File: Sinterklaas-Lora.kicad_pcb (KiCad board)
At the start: 2 copper layers, 80 x 100 mm, 1 part, among them U1 Pico

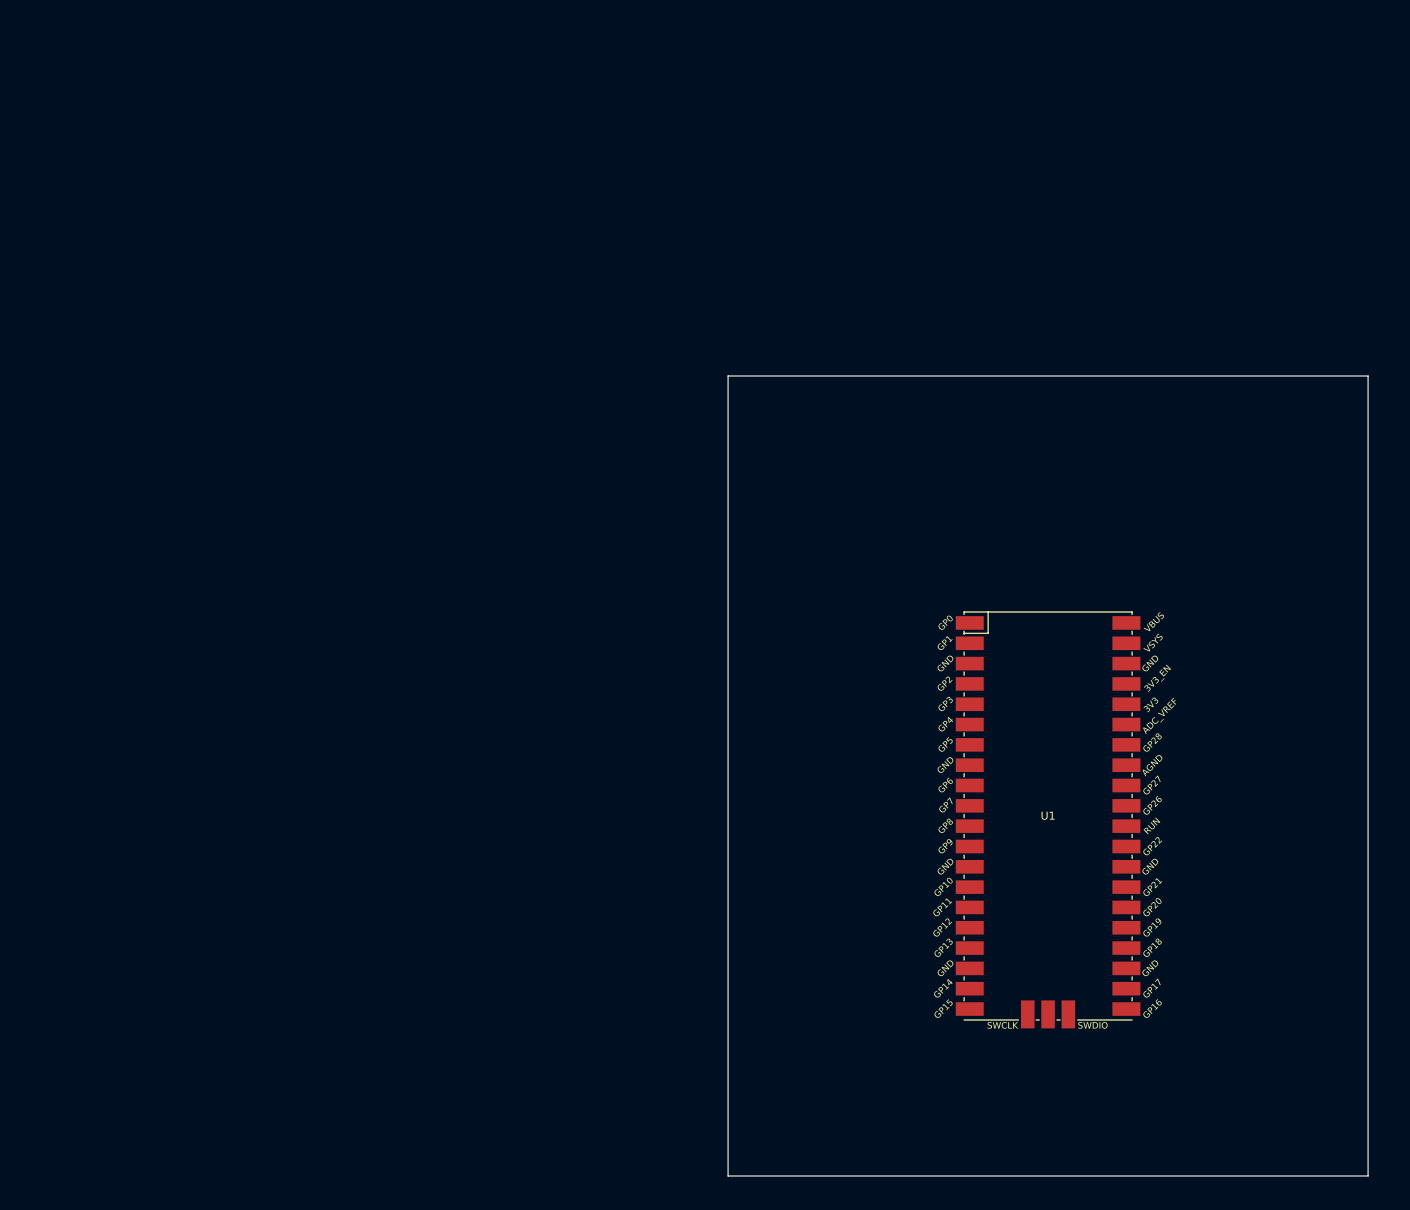
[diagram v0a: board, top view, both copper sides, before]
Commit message: Added battery holder
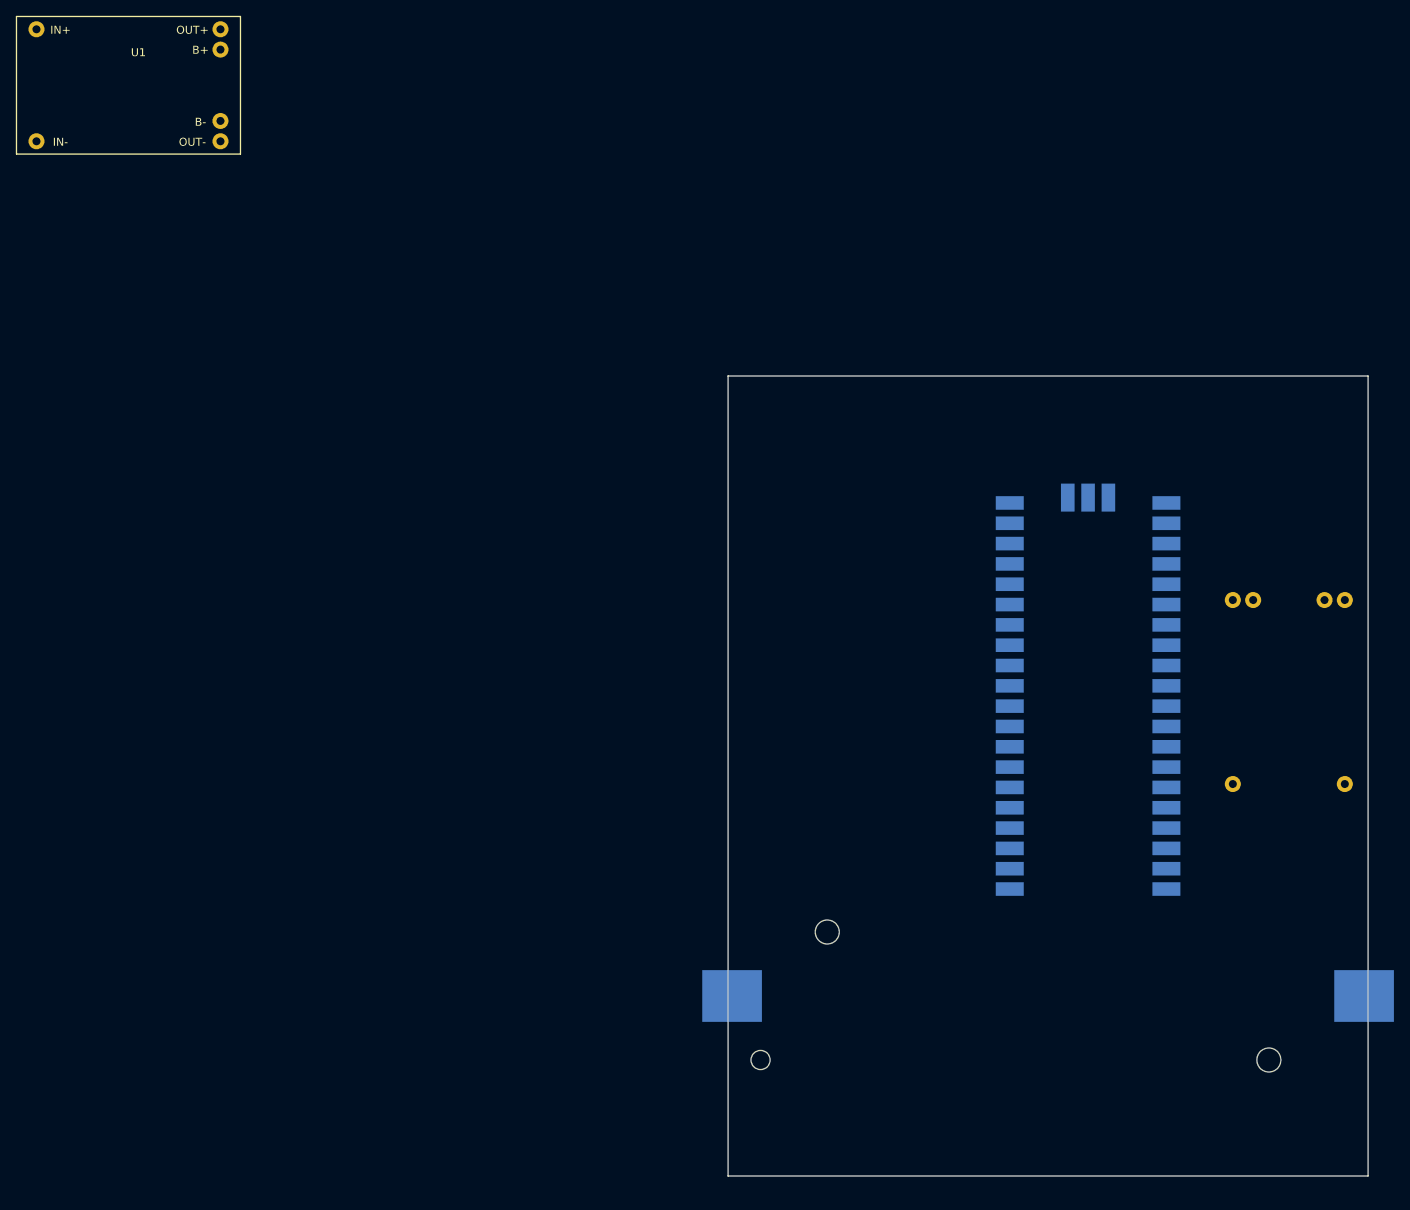
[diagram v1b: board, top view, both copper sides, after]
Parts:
- added BT1: Battery_Cell, Pi_pico:1042P, B.Cu at (172.5, 132.5)
- added U1: TP4056, Pi_pico:TP4056-Module, F.Cu at (1.05, 17.3)
- added U1: TP4056, Pi_pico:TP4056-Module, B.Cu at (151.5, 98.5)
- U2: renamed from U1; moved to B.Cu
- moved U2 15.8 mm to (135.0, 85.0)

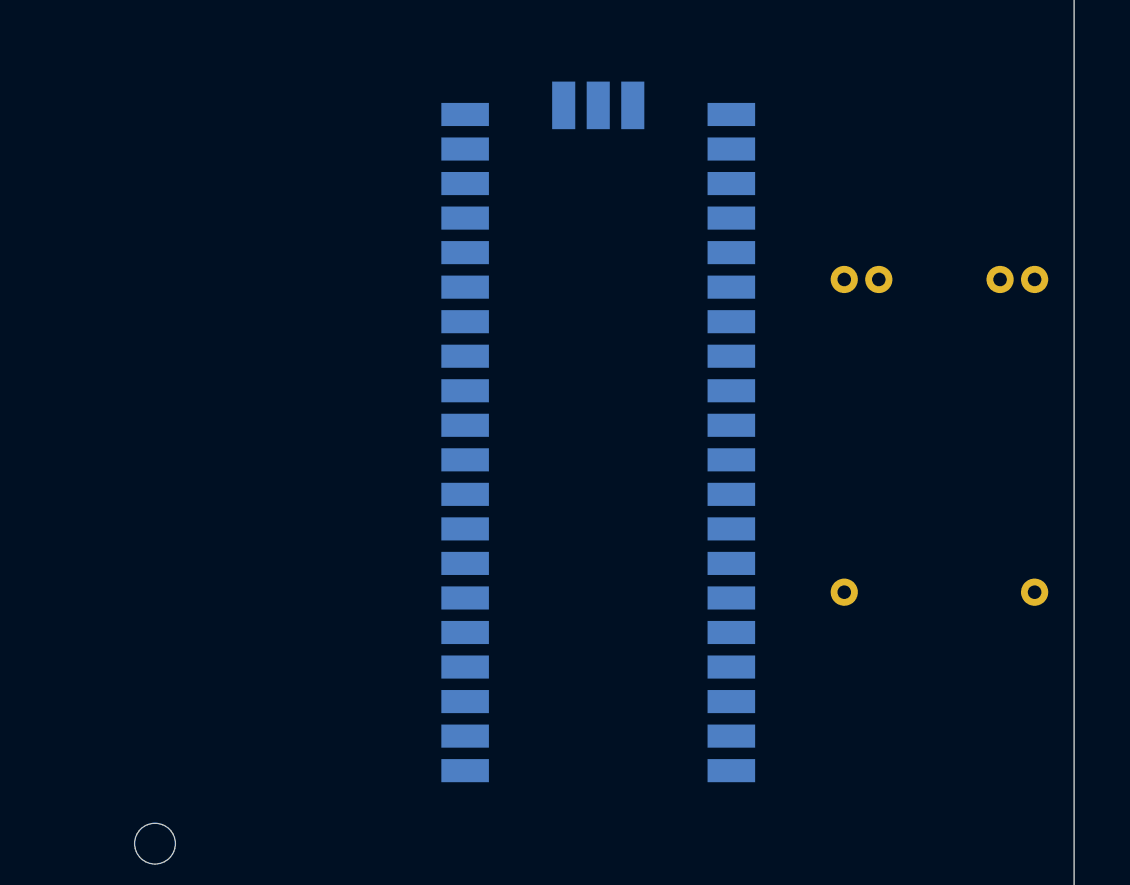
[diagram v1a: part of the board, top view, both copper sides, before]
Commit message: Added eByte E22-900M22S module to schematic
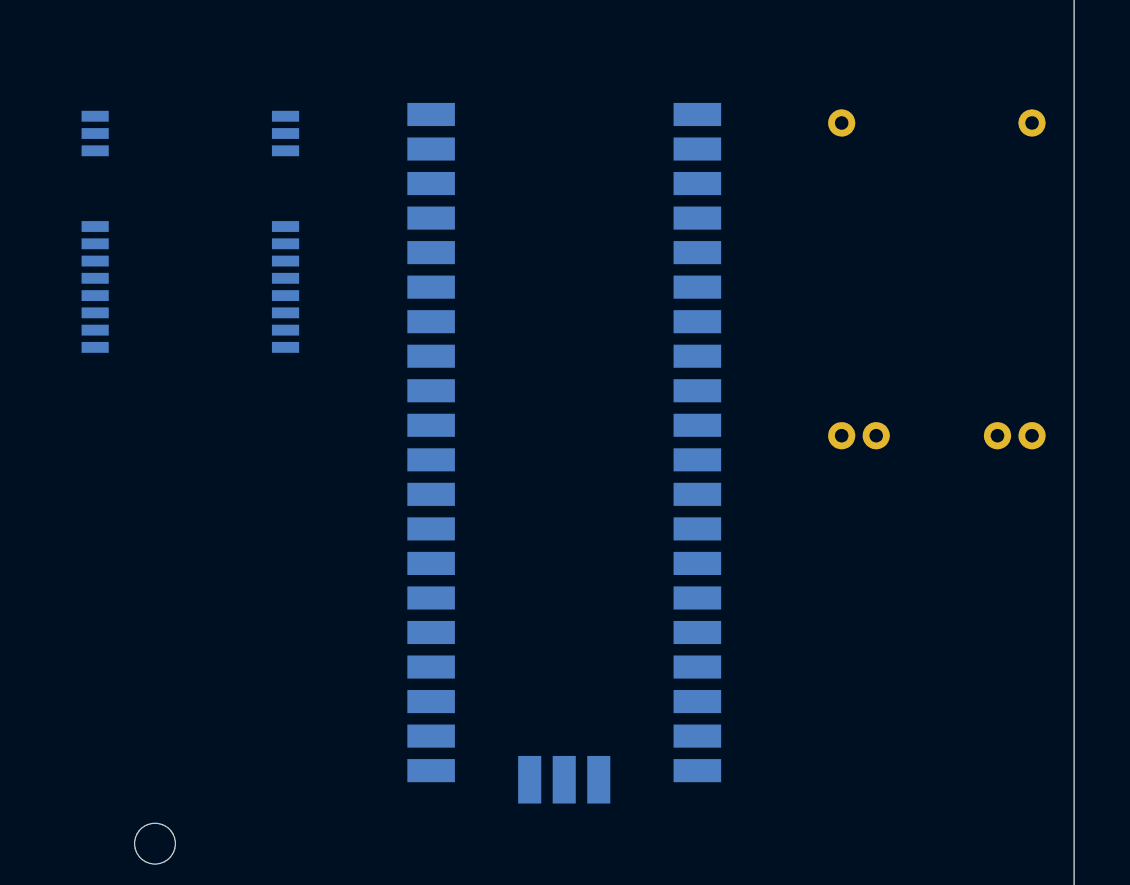
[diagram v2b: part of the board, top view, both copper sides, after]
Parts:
- added IC1: E22-900M22S, Pi_pico:E22-900M22S, B.Cu at (105.0, 70.0)
- moved U1 43.0 mm to (168.5, 59.0), turned to -90 degrees
- moved U2 2.50 mm to (132.5, 85.0), turned to 180 degrees
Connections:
- net Net-(BT1-Pad1) renamed VCC

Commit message: Added text
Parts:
- removed the U1 at (1.05, 17.3)
- added Q1: DMG2302U, Package_TO_SOT_SMD:SOT-23, B.Cu at (117.5, 62.5)
- moved U1 2.61 mm to (166.0, 59.7)
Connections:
- net VCC renamed Net-(BT1-Pad1)
- IC1 pad 1: Net-(IC1-Pad1) -> GND
- IC1 pad 10: Net-(IC1-Pad1) -> GND
- IC1 pad 11: Net-(IC1-Pad1) -> GND
- IC1 pad 12: Net-(IC1-Pad1) -> GND
- IC1 pad 13: unconnected-(IC1-Pad13) -> Net-(IC1-Pad13)
- IC1 pad 14: unconnected-(IC1-Pad14) -> Net-(IC1-Pad14)
- IC1 pad 16: unconnected-(IC1-Pad16) -> Net-(IC1-Pad16)
- IC1 pad 17: unconnected-(IC1-Pad17) -> Net-(IC1-Pad17)
- IC1 pad 18: unconnected-(IC1-Pad18) -> Net-(IC1-Pad18)
- IC1 pad 19: unconnected-(IC1-Pad19) -> Net-(IC1-Pad19)
- IC1 pad 2: Net-(IC1-Pad1) -> GND
- IC1 pad 20: Net-(IC1-Pad1) -> GND
- IC1 pad 22: Net-(IC1-Pad1) -> GND
- IC1 pad 3: Net-(IC1-Pad1) -> GND
- IC1 pad 4: Net-(IC1-Pad1) -> GND
- IC1 pad 5: Net-(IC1-Pad1) -> GND
- IC1 pad 6: unconnected-(IC1-Pad6) -> /RX_{EN}
- IC1 pad 7: unconnected-(IC1-Pad7) -> /TX_{EN}
- IC1 pad 8: unconnected-(IC1-Pad8) -> /DIO2
- IC1 pad 9: unconnected-(IC1-Pad9) -> +3.3V
- U2 pad 19: unconnected-(U2-Pad19) -> /~{RST}
- U2 pad 21: unconnected-(U2-Pad21) -> Net-(IC1-Pad13)
- U2 pad 22: unconnected-(U2-Pad22) -> Net-(IC1-Pad14)
- U2 pad 24: unconnected-(U2-Pad24) -> Net-(IC1-Pad16)
- U2 pad 25: unconnected-(U2-Pad25) -> Net-(IC1-Pad17)
- U2 pad 27: unconnected-(U2-Pad27) -> Net-(IC1-Pad18)
- U2 pad 29: unconnected-(U2-Pad29) -> Net-(IC1-Pad19)
- U2 pad 36: unconnected-(U2-Pad36) -> +3.3V
- U2 pad 39: unconnected-(U2-Pad39) -> +BATT
- U2 pad 40: unconnected-(U2-Pad40) -> +5V
- U2 pad 6: unconnected-(U2-Pad6) -> /RX_{EN}
- U2 pad 7: unconnected-(U2-Pad7) -> /TX_{EN}
- U2 pad 9: unconnected-(U2-Pad9) -> /DIO2
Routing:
- net Net-(BT1-Pad1): track 0.00 -> 154.5 mm
- net Net-(BT1-Pad2): track 0.00 -> 107.8 mm
- net Net-(IC1-Pad13): track 0.00 -> 44.9 mm
- net Net-(IC1-Pad14): track 0.00 -> 43.6 mm
- net Net-(IC1-Pad16): track 0.00 -> 41.0 mm
- net Net-(IC1-Pad17): track 0.00 -> 39.9 mm
- net +5V: track 0.00 -> 36.4 mm
- net Net-(IC1-Pad18): track 0.00 -> 36.1 mm
- net Net-(IC1-Pad19): track 0.00 -> 34.5 mm
- net /DIO2: track 0.00 -> 32.3 mm
- net /TX_{EN}: track 0.00 -> 30.7 mm
- net /RX_{EN}: track 0.00 -> 30.2 mm
- net +3.3V: track 0.00 -> 26.8 mm
- net GND: track 0.00 -> 24.5 mm
- net +BATT: track 0.00 -> 7.42 mm
- added copper zone on B.Cu, net GND
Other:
- board text added: "1.0"
- board text added: "Ik ben wat later vandaag"
- board text added: "Ik denk aan je"
- board text added: "Ja"
- board text added: "Kom je al naar huis?"
- board text added: "Kook jij vanavond?"
- board text added: "Nee"
- board text added: "Veel succes!"
- board text added: "Vergeet je x niet?"
- board text added: "Wasbeer communicator"

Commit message: another 3 hours of work
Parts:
- added D1: LED, Pi_pico:WL-SMDC, F.Cu at (99.2, 68.0)
- added D10: LED, LED_SMD:LED_0603_1608Metric_Pad1.05x0.95mm_HandSolder, F.Cu at (155.0, 92.0)
- added D11: LED, LED_SMD:LED_0603_1608Metric_Pad1.05x0.95mm_HandSolder, F.Cu at (155.0, 98.0)
- added D12: LED, LED_SMD:LED_0603_1608Metric_Pad1.05x0.95mm_HandSolder, F.Cu at (155.0, 95.0)
- added D13: LED, LED_SMD:LED_0603_1608Metric_Pad1.05x0.95mm_HandSolder, F.Cu at (155.0, 101.0)
- added D2: LED, Pi_pico:WL-SMDC, F.Cu at (99.2, 75.4)
- added D3: LED, Pi_pico:WL-SMDC, F.Cu at (99.2, 82.9)
- added D4: LED, Pi_pico:WL-SMDC, F.Cu at (99.2, 90.3)
- added D5: LED, Pi_pico:WL-SMDC, F.Cu at (99.2, 97.8)
- added D6: LED, Pi_pico:WL-SMDC, F.Cu at (99.2, 105.2)
- added D7: LED, Pi_pico:WL-SMDC, F.Cu at (99.2, 112.6)
- added D8: LED, Pi_pico:WL-SMDC, F.Cu at (99.2, 120.1)
- added D9: LED, Pi_pico:WL-SMDC, F.Cu at (99.2, 127.5)
- added R1: 390R, Resistor_SMD:R_1206_3216Metric, B.Cu at (156.0, 88.8)
- added SW1: SW_Push, Pi_pico:320.08E11wht, F.Cu at (154.0, 123.0)
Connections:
- IC1 pad 15: unconnected-(IC1-Pad15) -> /~{RST}
- U2 pad 10: unconnected-(U2-Pad10) -> /LED3
- U2 pad 11: unconnected-(U2-Pad11) -> /LED4
- U2 pad 12: unconnected-(U2-Pad12) -> /LED5
- U2 pad 14: unconnected-(U2-Pad14) -> /LED6
- U2 pad 15: unconnected-(U2-Pad15) -> /LED7
- U2 pad 16: unconnected-(U2-Pad16) -> /status
- U2 pad 17: unconnected-(U2-Pad17) -> /~{RST}
- U2 pad 19: /~{RST} -> /LED8
- U2 pad 2: unconnected-(U2-Pad2) -> /wifi
- U2 pad 20: unconnected-(U2-Pad20) -> /LED9
- U2 pad 26: unconnected-(U2-Pad26) -> /lora
- U2 pad 4: unconnected-(U2-Pad4) -> /LED1
- U2 pad 5: unconnected-(U2-Pad5) -> /LED2
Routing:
- net /~{RST}: track 0.00 -> 97.9 mm
- net /wifi: track 0.00 -> 88.1 mm, vias 0 -> 3
- net GND: track 24.5 -> 107.6 mm, vias 0 -> 4
- net /LED9: track 0.00 -> 78.7 mm, vias 0 -> 1
- net /LED2: track 0.00 -> 64.5 mm, vias 0 -> 1
- net +3.3V: track 26.8 -> 87.6 mm
- net /LED7: track 0.00 -> 56.4 mm, vias 0 -> 1
- net /LED8: track 0.00 -> 56.2 mm, vias 0 -> 1
- net /LED6: track 0.00 -> 51.8 mm, vias 0 -> 1
- net /LED1: track 0.00 -> 49.5 mm, vias 0 -> 1
- net /LED3: track 0.00 -> 49.5 mm, vias 0 -> 1
- net /LED5: track 0.00 -> 48.2 mm, vias 0 -> 1
- net /LED4: track 0.00 -> 45.0 mm, vias 0 -> 1
- net /lora: track 0.00 -> 33.0 mm, vias 0 -> 1
- net /DIO2: track 32.3 -> 60.9 mm
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- added copper zone on F.Cu, net GND
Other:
- board size 80 x 100 mm -> 83 x 100 mm
- board text added: "lorawan"
- board text added: "power"
- board text added: "status"
- board text added: "wifi"
